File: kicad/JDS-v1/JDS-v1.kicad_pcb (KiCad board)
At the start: 2 copper layers, 85 parts, among them J1 toPegMatrix, J10 mInJA, J11 mInJB, J12 Out, J13 Barrel_Jack_Switch, J2 fromPegsA, J3 fromPegsB, J4 fromPegsC, J5 fromPegsD, J6 fromPegsE, J7 fromPegsF, J8 fromPegsG, J9 fromPegsH, SW1 POW-SW, U1 74HC595, U2 LM7805_TO220

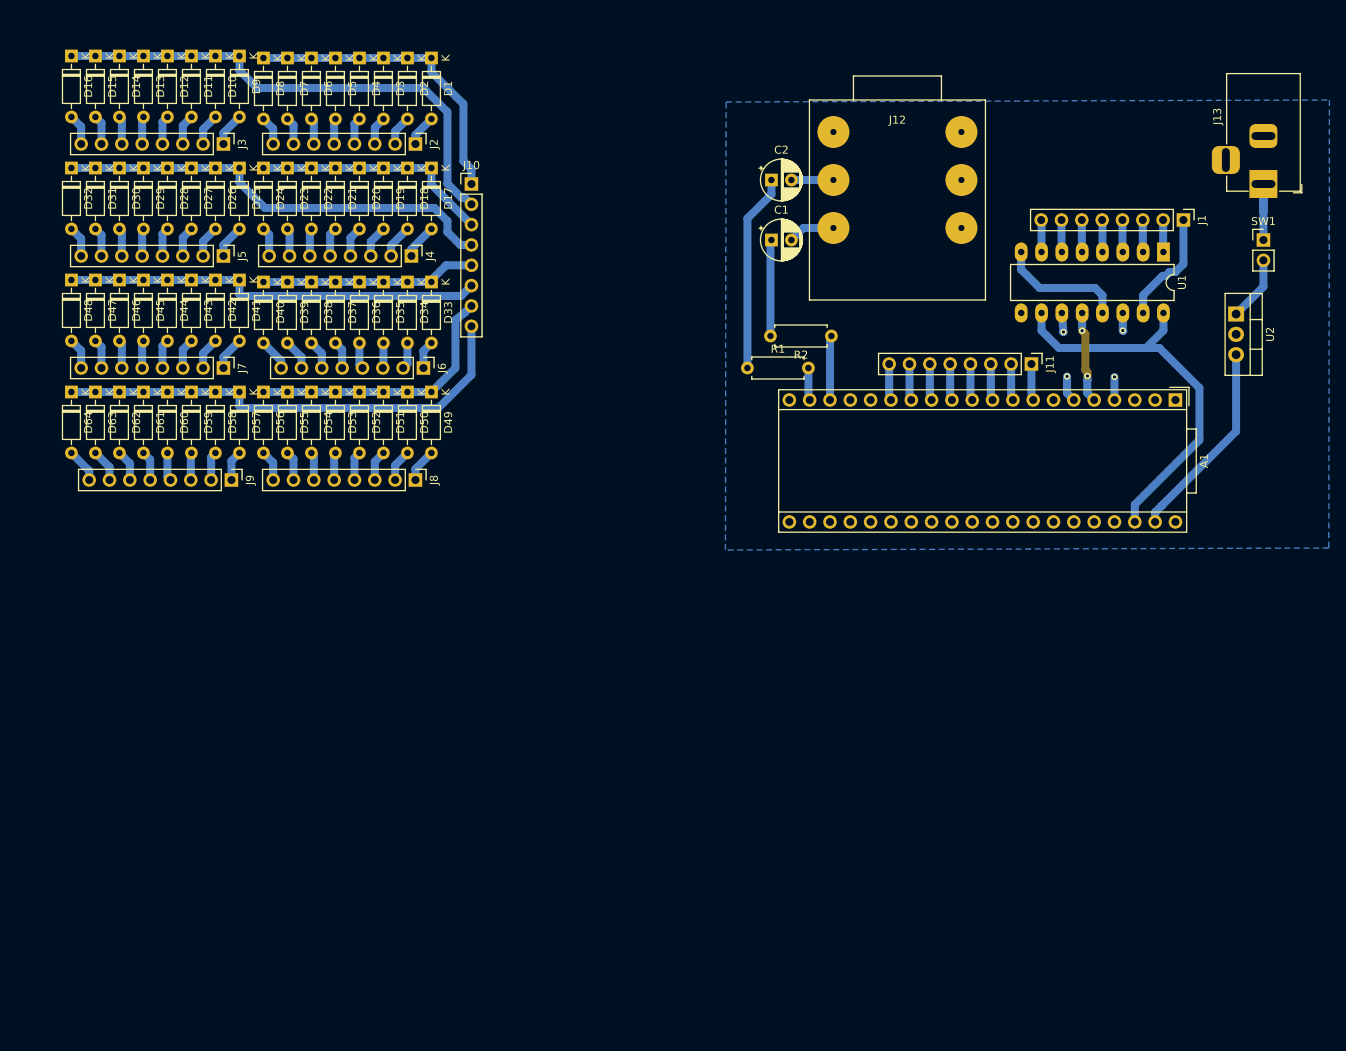
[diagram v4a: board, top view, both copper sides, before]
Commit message: changed connector footprints to RJ45
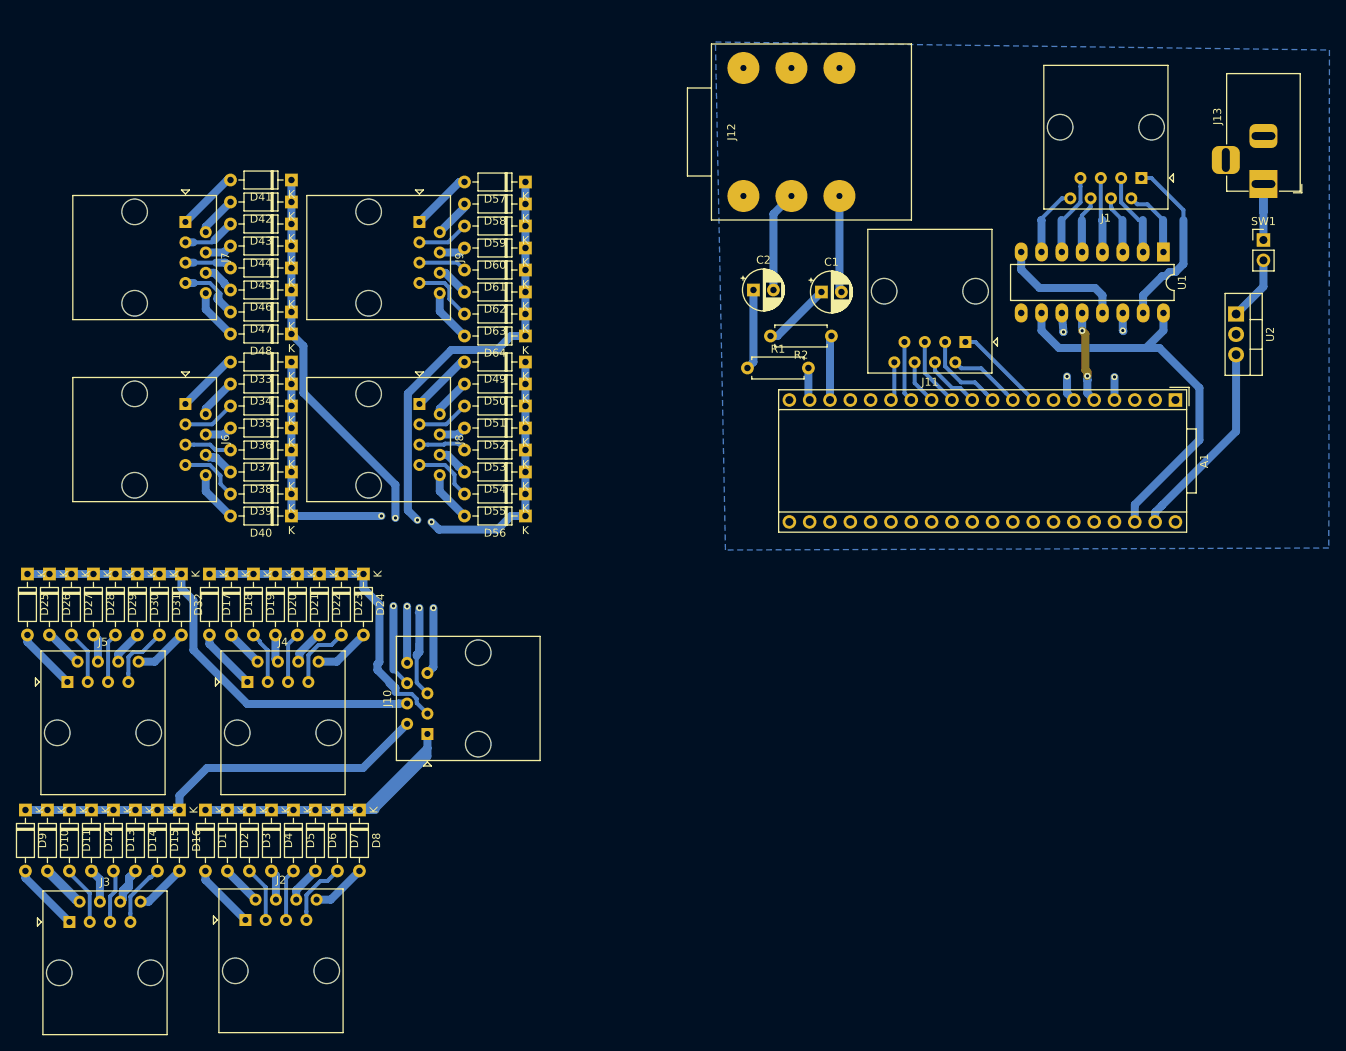
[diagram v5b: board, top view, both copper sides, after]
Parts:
- J1, J10, J11, J2, J3, J4, J5, J6, J7, J8, J9: footprint Connector_PinHeader_2.54mm:PinHeader_1x08_P2.54mm_Vertical -> Connector_RJ:RJ45_Amphenol_54602-x08_Horizontal
- moved J2 99.3 mm to (133.8, 162.0), turned to 0 degrees
- moved J3 99.1 mm to (111.8, 162.2), turned to 0 degrees
- moved D1 98.2 mm to (128.8, 148.2)
- moved D9 98.0 mm to (106.2, 148.2)
- moved D2 96.7 mm to (131.5, 148.2)
- moved D10 96.6 mm to (109.0, 148.2)
- moved D3 95.5 mm to (134.2, 148.2)
- moved D11 95.5 mm to (111.8, 148.2)
- moved D16 95.2 mm to (125.5, 148.2)
- moved D8 94.8 mm to (148.0, 148.2)
- moved D12 94.7 mm to (114.5, 148.2)
- moved D4 94.6 mm to (137.0, 148.2)
- moved D15 94.6 mm to (122.8, 148.2)
- moved D13 94.3 mm to (117.2, 148.2)
- moved D14 94.3 mm to (120.0, 148.2)
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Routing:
- net pm-in5: track 27.0 -> 48.6 mm, vias 0 -> 2
- net Net-(C2-Pad1): track 24.7 -> 10.1 mm
- net pm-in3: track 30.2 -> 42.7 mm
- net pm-in2: track 64.0 -> 53.2 mm
- net pm-out1: track 14.4 -> 22.5 mm
- net Net-(D10-Pad2): track 4.02 -> 11.7 mm
- net Net-(C2-Pad2): track 5.25 -> 12.7 mm
- net pm-in1: track 38.9 -> 46.3 mm
- net Net-(A1-Pad8): track 4.59 -> 11.5 mm
- net pm-out3: track 4.02 -> 10.7 mm
- net Net-(D47-Pad2): track 3.69 -> 10.3 mm
- net pm-in7: track 33.9 -> 40.5 mm, vias 0 -> 2
- net pm-out7: track 4.02 -> 10.3 mm
- net Net-(C1-Pad2): track 5.87 -> 12.1 mm
- net Net-(A1-Pad10): track 4.59 -> 10.7 mm
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
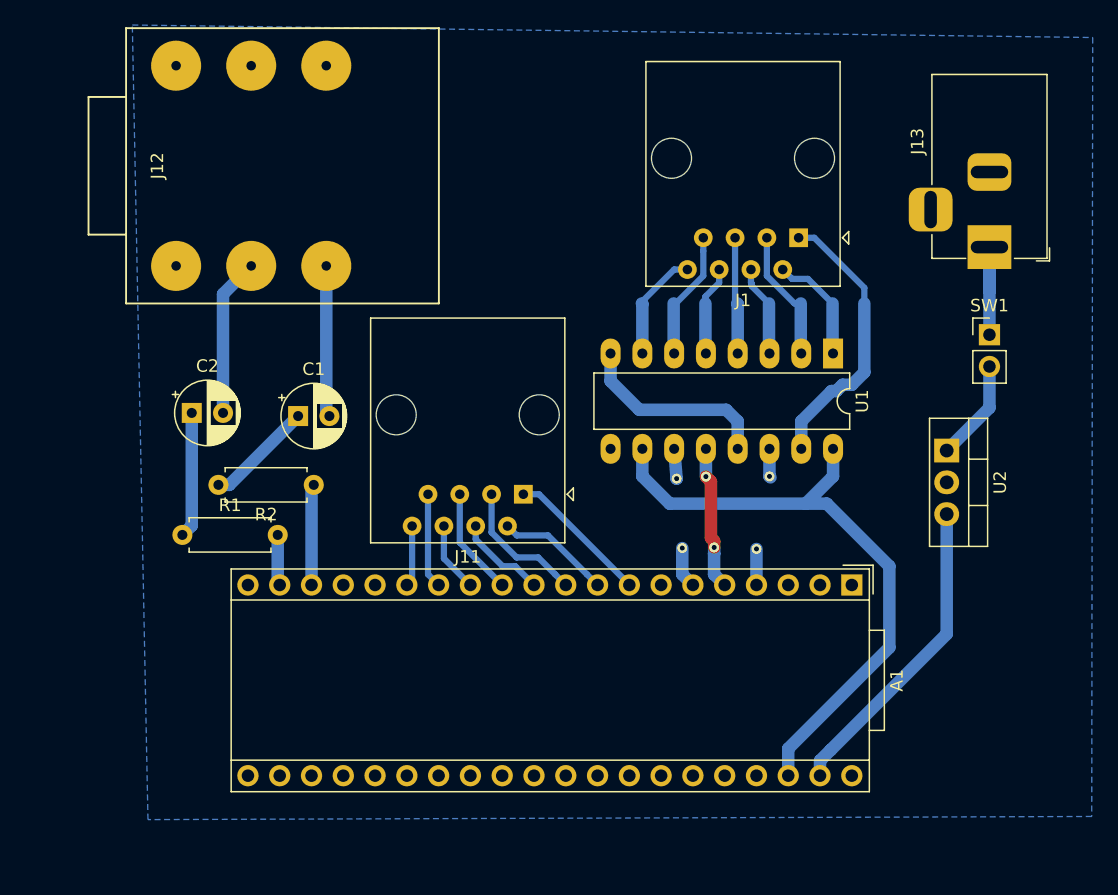
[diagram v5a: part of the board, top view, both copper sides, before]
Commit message: added pots to schmatic and pcb
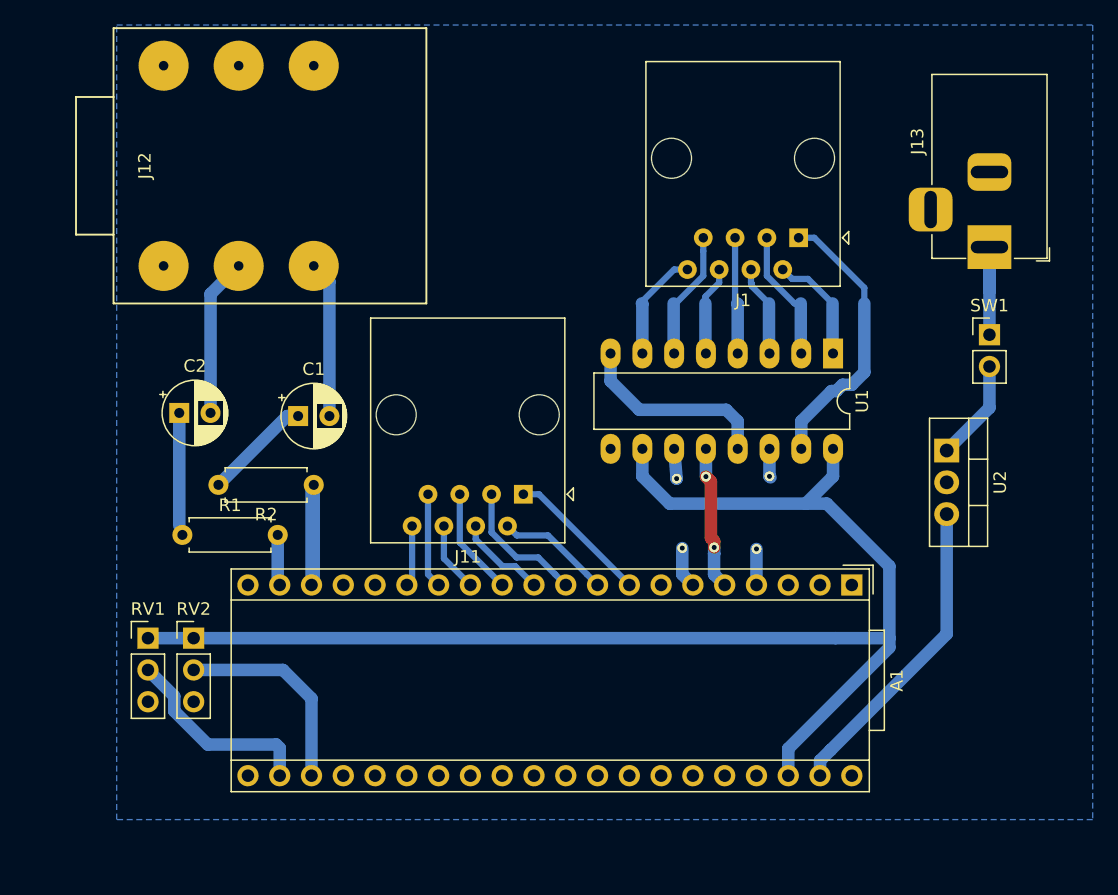
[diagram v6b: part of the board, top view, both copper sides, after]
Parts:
- added RV1: Vol, Connector_PinHeader_2.54mm:PinHeader_1x03_P2.54mm_Vertical, F.Cu at (193.8, 101.2)
- added RV2: Tempo, Connector_PinHeader_2.54mm:PinHeader_1x03_P2.54mm_Vertical, F.Cu at (197.4, 101.2)
- moved C2 1.00 mm to (196.2, 83.2)
- moved J12 1.00 mm to (193.0, 63.5)
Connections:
- A1 pad 23: Net-(A1-Pad23) -> pot2
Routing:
- net +3V3: track 50.3 -> 109.5 mm
- net pot2: track 0.00 -> 16.5 mm
- net pot1: track 0.00 -> 16.0 mm
- net toAmpL: track 8.07 -> 15.9 mm
- net Net-(C2-Pad1): track 10.1 -> 9.00 mm

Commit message: added pots and extra traces, print v2
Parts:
- moved RV1 4.81 mm to (193.0, 106.0), turned to 90 degrees
- moved RV2 4.54 mm to (193.0, 102.3), turned to 90 degrees
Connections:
- A1 pad 21: Net-(A1-Pad21) -> +3.3VA
- RV1 pad 1: +3V3 -> +3.3VA
- RV2 pad 1: +3V3 -> +3.3VA
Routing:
- net +3V3: track 109.5 -> 54.4 mm
- net +3.3VA: track 0.00 -> 21.1 mm
- net +5V: track 25.3 -> 29.5 mm
- net Net-(A1-Pad28): track 0.00 -> 3.49 mm
- net Net-(A1-Pad29): track 0.00 -> 3.45 mm
- net Net-(A1-Pad32): track 0.00 -> 3.44 mm
- net Net-(A1-Pad30): track 0.00 -> 3.41 mm
- net Net-(A1-Pad31): track 0.00 -> 3.35 mm
- net Net-(A1-Pad34): track 0.00 -> 3.25 mm
- net Net-(A1-Pad27): track 0.00 -> 3.24 mm
- net Net-(A1-Pad33): track 0.00 -> 3.23 mm
- net Net-(A1-Pad35): track 0.00 -> 3.21 mm
- net Net-(A1-Pad36): track 0.00 -> 3.17 mm
- net Net-(A1-Pad37): track 0.00 -> 3.13 mm
- net Net-(A1-Pad24): track 0.00 -> 3.12 mm
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
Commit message: added ethernet mounting PCBs and v3 print
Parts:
- added J14: swOutJump, Connector_PinHeader_2.54mm:PinHeader_1x08_P2.54mm_Vertical, F.Cu at (202.5, 144.0)
- added J15: swOut, Connector_RJ:RJ45_Amphenol_54602-x08_Horizontal, F.Cu at (195.0, 148.5)
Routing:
- net Net-(J14-Pad1): track 0.00 -> 9.36 mm
- net Net-(J14-Pad7): track 0.00 -> 9.10 mm
- net Net-(J14-Pad3): track 0.00 -> 8.30 mm
- net Net-(J14-Pad5): track 0.00 -> 7.91 mm
- net Net-(J14-Pad8): track 0.00 -> 6.78 mm
- net Net-(J14-Pad2): track 0.00 -> 6.30 mm
- net Net-(J14-Pad6): track 0.00 -> 5.73 mm
- net Net-(J14-Pad4): track 0.00 -> 5.33 mm
